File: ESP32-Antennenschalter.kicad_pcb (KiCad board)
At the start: 2 copper layers, 160.2 x 104.1 mm, 117 parts, among them J1 IN1(TRX1), J10 T1_In, J11 T1_Out, J12 T2_Out, J13 T2_In, J14 Tuner/Ext_TRX, J15 Tuner/Ext_ANT, J16 L2, J17 L2, J18 L2, J19 L2, J2 IN2(TRX2), J20 L2, J21 L2, J22 L2, J23 L2, J24 MCP_Addr, J25 ADC2, J26 ADC3, J27 Ext, J28 ADC_Addr, J3 IN3(RX), J4 ANT1, J5 ANT2, J6 ANT3, J7 ANT4, J8 ANT-DUMMY, J9 ANT-RX, K1 Finder 40.31.6.006.0000, K10 Finder 40.31.6.006.0000, K11 Finder 40.31.6.006.0000, K12 Finder 40.31.6.006.0000, K13 Finder 40.31.6.006.0000, K14 Finder 40.31.6.006.0000, K15 Finder 40.31.6.006.0000, K16 Finder 40.31.6.006.0000, K2 Finder 40.31.6.006.0000, K3 Finder 40.31.6.006.0000, K4 Finder 40.31.6.006.0000, K5 Finder 40.31.6.006.0000, K6 Finder 40.31.6.006.0000, K7 Finder 40.31.6.006.0000, K8 Finder 40.31.6.006.0000, K9 Finder 40.31.6.006.0000, SW1 Input, SW2 Output, U2 DRV8833PWP, U3 DRV8833PWP, U4 MCP23017_SO, U5 DRV8833PWP, U6 DRV8833PWP, U7 ADS1115IDGS, U8 Wemos D1 mini ESP32

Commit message: Add files via upload
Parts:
- added J29: Conn_01x01_Pin, Connector_Pin:Pin_D0.7mm_L6.5mm_W1.8mm_FlatFork, F.Cu at (162.2, 109.0)
- added J30: Conn_01x01_Pin, Connector_Pin:Pin_D0.7mm_L6.5mm_W1.8mm_FlatFork, F.Cu at (106.4, 95.3)
- added J31: Conn_01x01_Pin, Connector_Pin:Pin_D0.7mm_L6.5mm_W1.8mm_FlatFork, F.Cu at (179.2, 66.3)
- added J32: Conn_01x01_Pin, Connector_Pin:Pin_D0.7mm_L6.5mm_W1.8mm_FlatFork, F.Cu at (43.0, 71.4)
- added J33: Conn_01x01_Pin, Connector_Pin:Pin_D0.7mm_L6.5mm_W1.8mm_FlatFork, F.Cu at (147.5, 97.9)
- added J34: Conn_01x01_Pin, Connector_Pin:Pin_D0.7mm_L6.5mm_W1.8mm_FlatFork, F.Cu at (120.7, 107.2)
- added J35: Conn_01x01_Pin, Connector_Pin:Pin_D0.7mm_L6.5mm_W1.8mm_FlatFork, F.Cu at (97.3, 86.4)
- added J36: Conn_01x01_Pin, Connector_Pin:Pin_D0.7mm_L6.5mm_W1.8mm_FlatFork, F.Cu at (50.4, 87.5)
- added J37: Conn_01x01_Pin, Connector_Pin:Pin_D0.7mm_L6.5mm_W1.8mm_FlatFork, F.Cu at (94.0, 107.0)
- added J38: Conn_01x01_Pin, Connector_Pin:Pin_D0.7mm_L6.5mm_W1.8mm_FlatFork, F.Cu at (80.5, 122.6)
- added J39: Conn_01x01_Pin, Connector_Pin:Pin_D0.7mm_L6.5mm_W1.8mm_FlatFork, F.Cu at (115.7, 76.8)
- added J40: Conn_01x01_Pin, Connector_Pin:Pin_D0.7mm_L6.5mm_W1.8mm_FlatFork, F.Cu at (63.1, 76.7)
- added J41: Conn_01x01_Pin, Connector_Pin:Pin_D0.7mm_L6.5mm_W1.8mm_FlatFork, F.Cu at (170.7, 77.1)
- added J42: Conn_01x01_Pin, Connector_Pin:Pin_D0.7mm_L6.5mm_W1.8mm_FlatFork, F.Cu at (143.8, 76.7)
- added J43: Conn_01x01_Pin, Connector_Pin:Pin_D0.7mm_L6.5mm_W1.8mm_FlatFork, F.Cu at (126.1, 88.0)
- added J44: Conn_01x01_Pin, Connector_Pin:Pin_D0.7mm_L6.5mm_W1.8mm_FlatFork, F.Cu at (157.8, 88.1)
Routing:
- net Net-(U3-BOUT1): track 72.1 -> 73.5 mm
- net Net-(U3-BOUT2): track 75.3 -> 76.4 mm

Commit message: added vias for better shielding
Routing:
- net GND: vias 0 -> 62
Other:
- board text added: "JLCJLCJLCJLC"

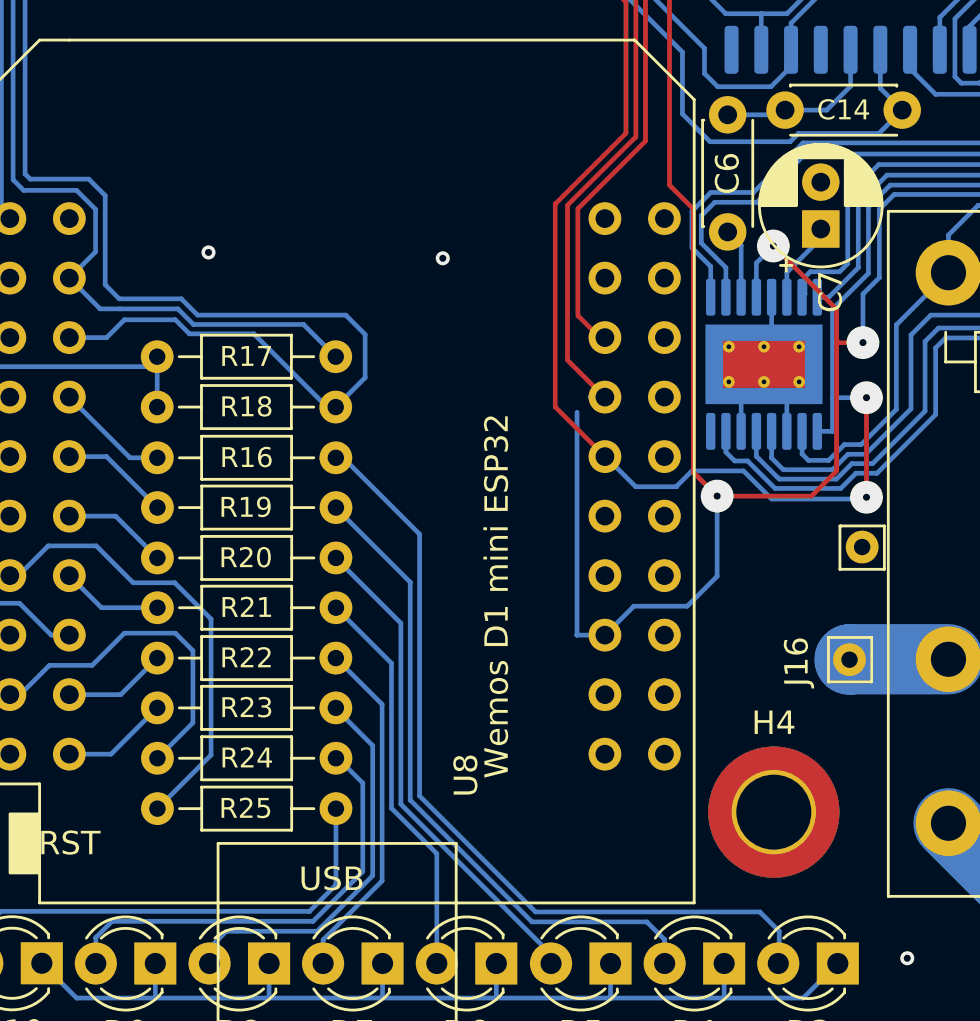
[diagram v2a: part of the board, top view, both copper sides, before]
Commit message: repaired broken GND-connection of U2
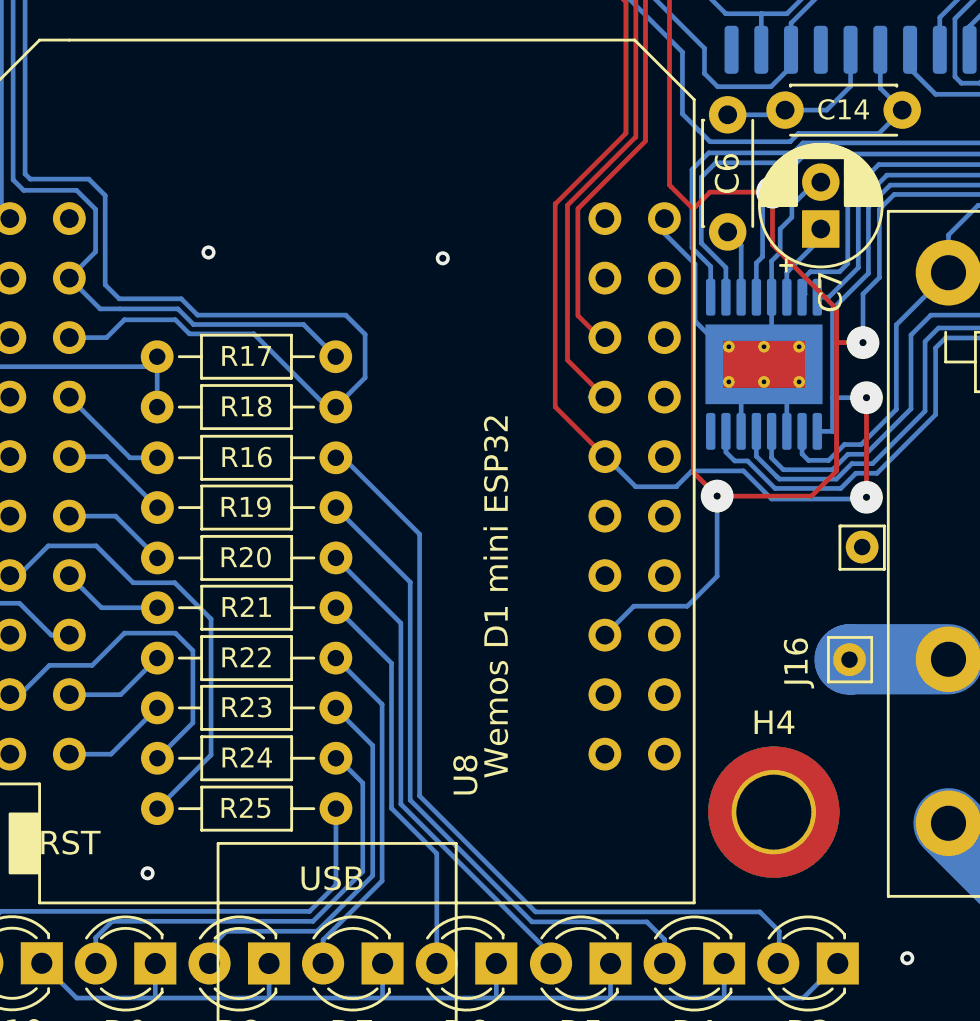
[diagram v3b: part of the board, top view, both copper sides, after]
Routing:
- net GND: track 220.6 -> 233.4 mm, vias 62 -> 63
- net +5V: track 252.9 -> 250.5 mm
- net Net-(U2-BIN1): track 24.1 -> 25.2 mm
- net Net-(U2-BIN2): track 28.8 -> 29.8 mm

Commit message: SWR-Meter: Remove R11,R23; Replace R4,R5 with 8.2K
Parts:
- R11, R12: value 100k -> REMOVE
- R4, R5: value 100k -> 8.2k
